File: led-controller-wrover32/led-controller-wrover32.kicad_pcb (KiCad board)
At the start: 2 copper layers, 36 x 36 mm, 54 parts, among them J1 Micro_SD_Card, J2 Conn_01x12, J3 USB_B_Micro, J4 Conn_01x12, J5 Conn_01x04 DNS, J6 Conn_01x02 DNS, J7 Conn_01x03 DNS, J8 Conn_01x05, Q1 MMDT5551, Q2 MMBT2222A-TP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

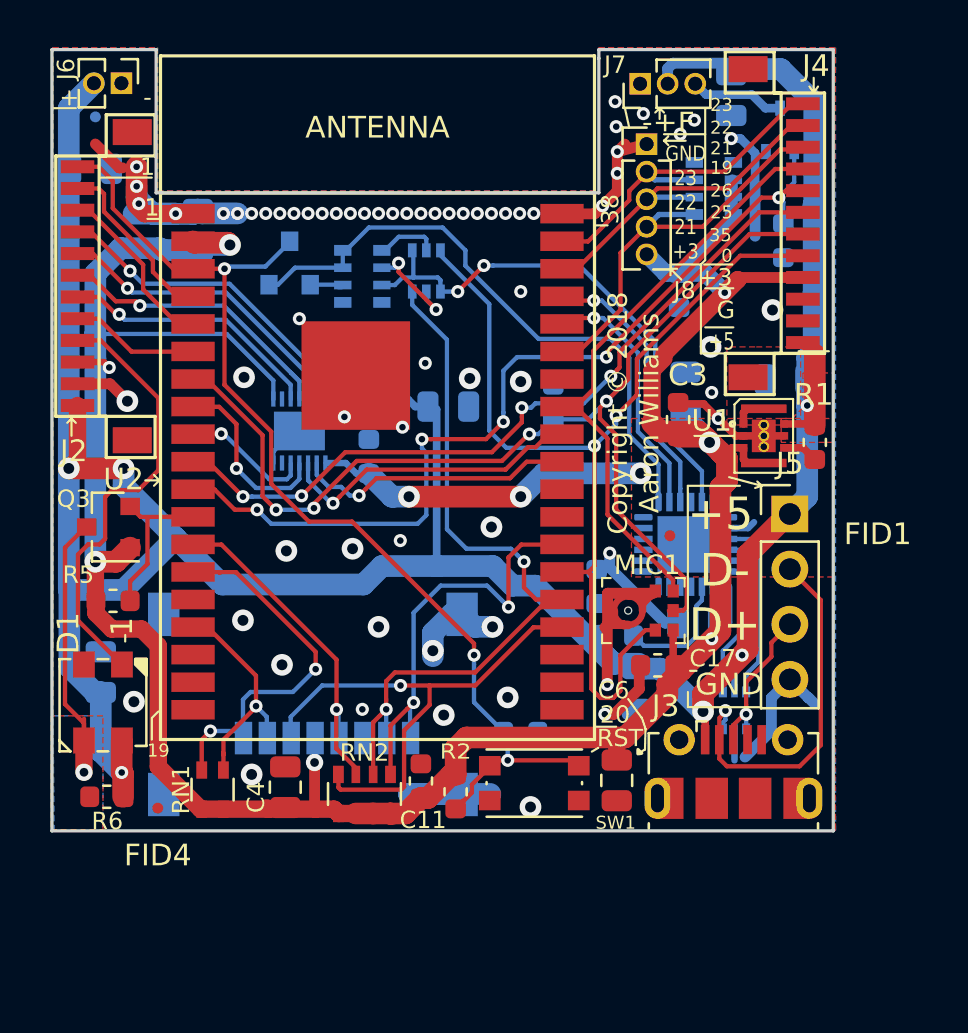
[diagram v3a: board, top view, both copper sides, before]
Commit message: Added 12v boost supply and enlarged board.
This branch and initial commit enlarges the board in order to add a 5V to
12V boost switching supply which can provide up to 400ma of current.

Additionally, J5 was changed to a JST PH connector and J9 and J101 were
added.  All 12V boost supply components start at 100.  Due to the
addition of the boost switching supply, the length of the board was
increased.

In addition, some more filtering capacitors were added and some key traces
for +5V from J9 and J5 were increased to handle additional current for
the 12v supply.

The 12v boost circuit has already been tested and verified to work.

The revision of this branch has been switched to 2.0.0.

Signed-off-by: Aaron Williams <aaron.w2@gmail.com>
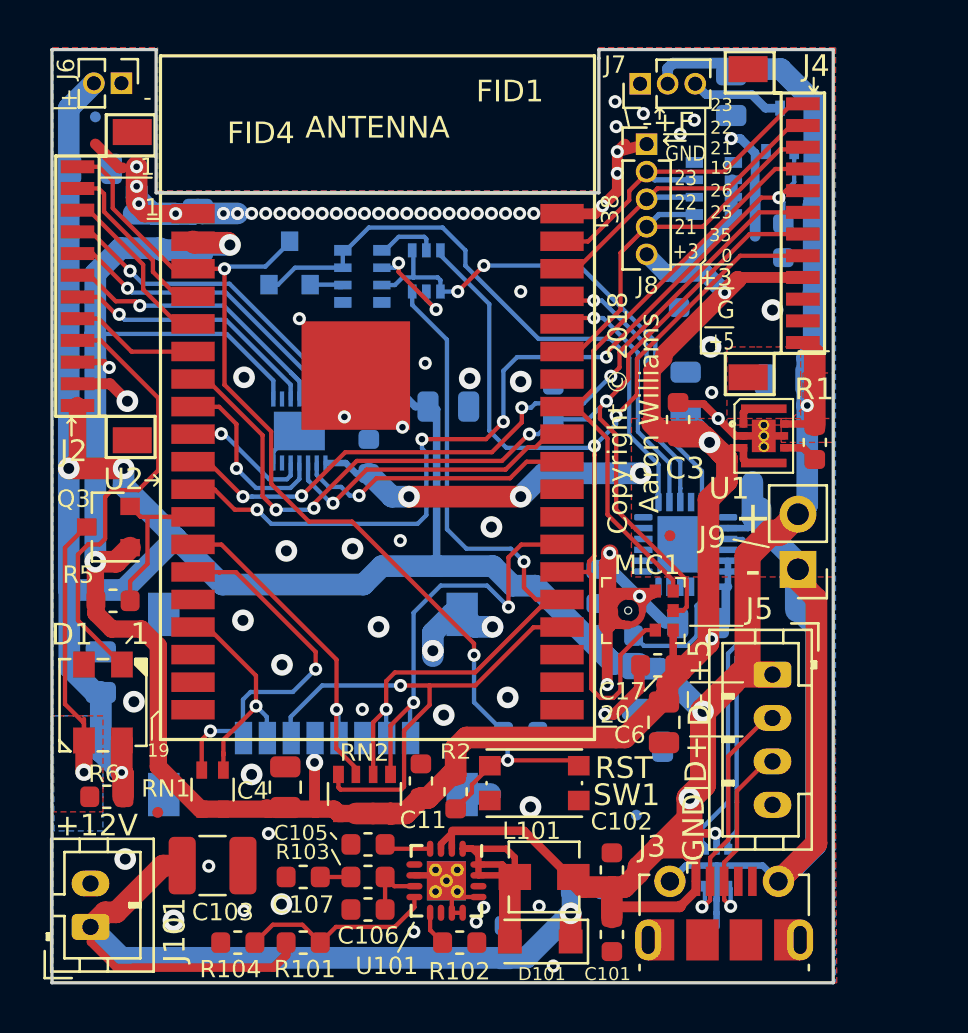
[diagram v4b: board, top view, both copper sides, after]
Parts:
- added C101: 6.8uF, Capacitor_SMD:C_0603_1608Metric, F.Cu at (75.8, 82.8)
- added C102: 100nF, Capacitor_SMD:C_0603_1608Metric, F.Cu at (75.8, 79.8)
- added C103: 22uF, Capacitor_SMD:C_1210_3225Metric, F.Cu at (57.4, 79.6)
- added C104: 1uF, Capacitor_SMD:C_0603_1608Metric, B.Cu at (74.7, 80.7)
- added C105: 22nF, Capacitor_SMD:C_0603_1608Metric, F.Cu at (64.6, 78.6)
- added C106: 820pF, Capacitor_SMD:C_0603_1608Metric, F.Cu at (64.6, 81.6)
- added C107: 47nF, Capacitor_SMD:C_0603_1608Metric, F.Cu at (61.6, 80.1)
- added C108: 0.1uF, Capacitor_SMD:C_0603_1608Metric, B.Cu at (70.9, 83.2)
- added C19: 10uF, Capacitor_SMD:C_0805_2012Metric, B.Cu at (79.1, 74.1)
- added D101: D_Schottky, Diode_SMD:D_SOD-123F, F.Cu at (72.5, 83.1)
- added J101: Conn_01x02 DNS, Connector_JST:JST_PH_B2B-PH-K_1x02_P2.00mm_Vertical, F.Cu at (51.8, 82.4)
- added J9: Conn_01x02 DNS, Connector_PinHeader_2.54mm:PinHeader_1x02_P2.54mm_Vertical, F.Cu at (84.4, 66.0)
- added L101: 3.3uH, Aaron:L_Vishay_IHLP-1212, F.Cu at (72.7, 80.1)
- added R101: 86.6k, Resistor_SMD:R_0603_1608Metric, F.Cu at (61.6, 83.2)
- added R102: 18.2k, Resistor_SMD:R_0603_1608Metric, F.Cu at (68.8, 83.2)
- added R103: 1.69k, Resistor_SMD:R_0603_1608Metric, F.Cu at (64.6, 80.1)
- added R104: 10k, Resistor_SMD:R_0603_1608Metric, F.Cu at (58.6, 83.2)
- added U101: TPS55340-Q1, Aaron:QFN-16-1EP_3x3mm_P0.5mm_EP2.7x2.7mm_ThermalVias, F.Cu at (68.2, 80.3)
- J1: footprint Connector_Card:microSD_HC_Wuerth_693072010801 -> Aaron:microSD_HC_Wuerth_693072010801
- J5: footprint Connector_PinHeader_2.54mm:PinHeader_1x04_P2.54mm_Vertical -> Connector_JST:JST_PH_B4B-PH-K_1x04_P2.00mm_Vertical
- moved J5 7.44 mm to (83.2, 70.8), turned to 270 degrees
- moved D2 7.30 mm to (80.6, 79.7)
- moved J3 6.54 mm to (81.0, 81.8)
- moved FID2 5.28 mm to (76.9, 77.3)
- moved C6 3.45 mm to (78.2, 73.0)
- moved FID4 0.20 mm to (54.9, 77.2)
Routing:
- net GND: track 76.8 -> 119.6 mm, vias 67 -> 79
- net +12V: track 0.00 -> 42.4 mm, vias 0 -> 1
- net VBUS: track 141.8 -> 179.1 mm, vias 6 -> 7
- net /12v-booster/SW: track 0.00 -> 11.9 mm
- net /12v-booster/FB: track 0.00 -> 9.18 mm
- net /USB_D-: track 7.62 -> 15.5 mm
- net /USB_D+: track 8.46 -> 15.8 mm
- net /D-: track 17.2 -> 11.3 mm
- net /12v-booster/COMP: track 0.00 -> 3.03 mm
- net /12v-booster/SS: track 0.00 -> 2.16 mm
- net /D+: track 7.18 -> 8.98 mm
- net /12v-booster/FREQ: track 0.00 -> 1.61 mm
- net Net-(C107-Pad1): track 0.00 -> 1.41 mm
- net +3V3: track 144.9 -> 143.9 mm
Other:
- board size 36 x 36 mm -> 36 x 43 mm
- board text added: "+ -"
- board text added: "+12V"
- board text added: "-GND +12V"
- board text added: "Rev 2.0.0"
- board text removed: "Rev 1.5.0"

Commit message: Added BOM and also fixed missing value for RN3
Signed-off-by: Aaron Williams <aaron.w2@gmail.com>
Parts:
- RN3: value R_Pack04 -> 10K
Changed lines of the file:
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@@
   )
   (setup
-    (last_trace_width 1)
+    (last_trace_width 0.2)
     (user_trace_width 0.2)
     (user_trace_width 0.25)
@@
       (effects (font (size 1 1) (thickness 0.15)) (justify mirror))
     )
-    (fp_text value R_Pack04 (at 0 -2.8) (layer B.Fab)
-      (effects (font (size 1 1) (thickness 0.15)) (justify mirror))
-    )
+    (fp_text value 10K (at 0 -2.8) (layer B.Fab)
+      (effects (font (size 1 1) (thickness 0.15)) (justify mirror))
+    )

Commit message: Fixed solder mask padding.
Signed-off-by: Aaron Williams <aaron.w2@gmail.com>
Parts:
- D2: value USBLC6-2SC6 -> USBLC6-2P6
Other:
- board text added: "Rev 2.0.2"
- board text removed: "Rev 2.0.0"
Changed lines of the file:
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@@
-(kicad_pcb (version 20171130) (host pcbnew 5.0.1-5.0.1)
+(kicad_pcb (version 20171130) (host pcbnew 5.0.2-5.0.2)
   (general
     (thickness 1.6)
-    (drawings 86)
+    (drawings 87)
     (tracks 988)
     (zones 0)
@@
   (title_block
     (title "Wrover LED Controller")
-    (date 2018-11-10)
-    (rev 2.0)
+    (date 2019-01-25)
+    (rev 2.0.2)
     (company "Copyright 2018 by Aaron Williams")
   )
@@
     (pad_to_mask_clearance 0.0508)
     (solder_mask_min_width 0.25)
+    (pad_to_paste_clearance -0.0504)
     (aux_axis_origin 0 0)
     (visible_elements FFFFFFFF)
@@
       (effects (font (size 1 1) (thickness 0.15)) (justify mirror))
     )
-    (fp_text value USBLC6-2SC6 (at 0 -1.75 -90) (layer B.Fab)
+    (fp_text value USBLC6-2P6 (at 0 -1.75 -90) (layer B.Fab)
       (effects (font (size 1 1) (thickness 0.15)) (justify mirror))
     )
@@
     )
   )
+  (gr_circle (center 81.675 81.075) (end 81.7 81.125) (layer B.SilkS) (width 0.1))
   (gr_line (start 81.4 64.575) (end 83.025 64.925) (layer F.SilkS) (width 0.1))
   (gr_text "+\n-" (at 82.3 64.775) (layer F.SilkS)
@@
     (effects (font (size 0.8 0.8) (thickness 0.1)))
   )
-  (gr_text "Rev 2.0.0" (at 64.75 83.45) (layer B.SilkS)
+  (gr_text "Rev 2.0.2" (at 64.75 83.45) (layer B.SilkS)
     (effects (font (size 1.5 1.5) (thickness 0.25)) (justify mirror))
   )

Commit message: Oops, changed the wrong thing, this fixes it.
Signed-off-by: Aaron Williams <aaron.w2@gmail.com>
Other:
- rule pad_to_mask_clearance: 0.0508 -> -0.0508
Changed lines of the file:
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@@
   )
   (layers
-    (0 F.Cu signal)
+    (0 F.Cu signal hide)
     (31 B.Cu signal)
     (32 B.Adhes user)
@@
     (pad_size 1.2 1.75)
     (pad_drill 0.75)
-    (pad_to_mask_clearance 0.0508)
+    (pad_to_mask_clearance -0.0508)
     (solder_mask_min_width 0.25)
-    (pad_to_paste_clearance -0.0504)
     (aux_axis_origin 0 0)
     (visible_elements FFFFFFFF)
